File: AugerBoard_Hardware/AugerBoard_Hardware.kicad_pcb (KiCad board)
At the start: 2 copper layers, 88.9 x 82.5 mm, 51 parts, among them J1 RJ45_LED_Shielded, J2 Conn_01x04_MountingPin, Q1 BSS138, Q2 BSS138, Q3 BSS138, SW1 SW_SPDT, SW2 SW_Push, SW3 SW_Push, SW4 SW_Push, U1 Teensy4.1_DEV-16771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

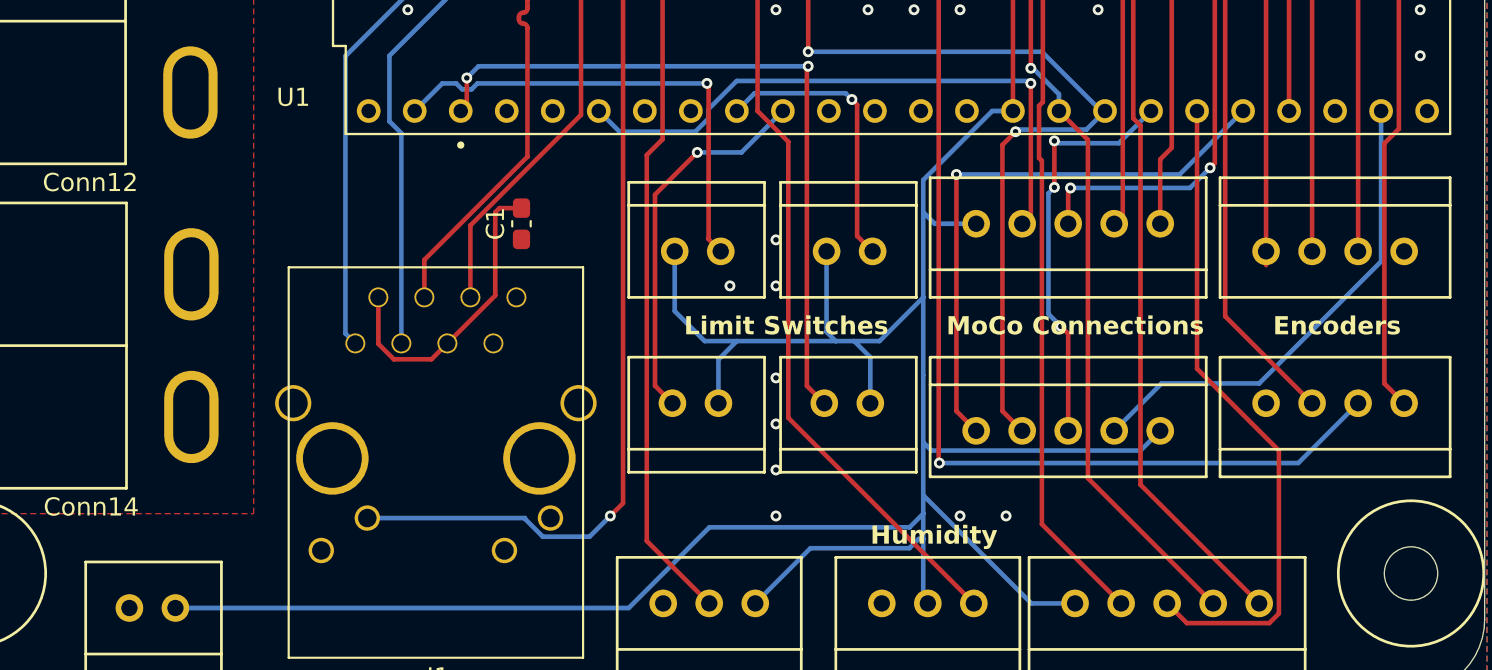
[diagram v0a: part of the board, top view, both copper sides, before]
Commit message: Flipped moco connector and traces, and added labels
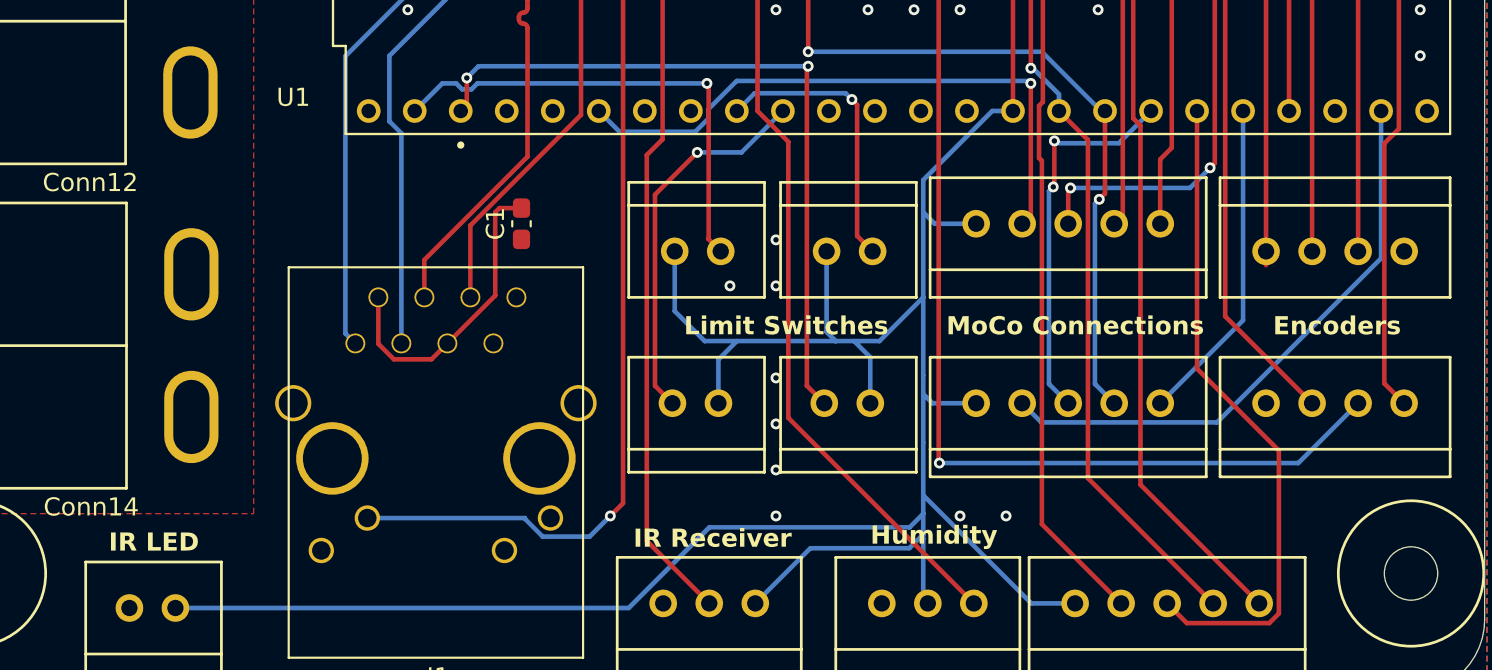
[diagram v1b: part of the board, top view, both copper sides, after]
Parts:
- moved Conn13 10.3 mm to (145.7, 138.6), turned to 180 degrees
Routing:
- net IN_B2: track 32.3 -> 18.5 mm, vias 1 -> 0
- net +3.3V: track 288.0 -> 277.5 mm
- net PWM2: track 81.4 -> 75.6 mm
- net IN_A2: track 26.9 -> 32.1 mm
- net CS2: track 22.7 -> 21.2 mm, vias 3 -> 2
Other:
- board text added: "IR LED"
- board text added: "IR Receiver"

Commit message: Flipped other moco gg
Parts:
- moved Conn9 10.3 mm to (135.5, 130.2), turned to 0 degrees
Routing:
- net +3.3V: track 277.5 -> 288.3 mm
- net IN_B1: track 39.1 -> 49.4 mm, vias 1 -> 3
- net IN_A1: track 33.8 -> 39.7 mm
- net PWM1: track 85.8 -> 82.5 mm
- net CS1: track 29.1 -> 31.4 mm
- net PWM3: track 76.3 -> 76.9 mm

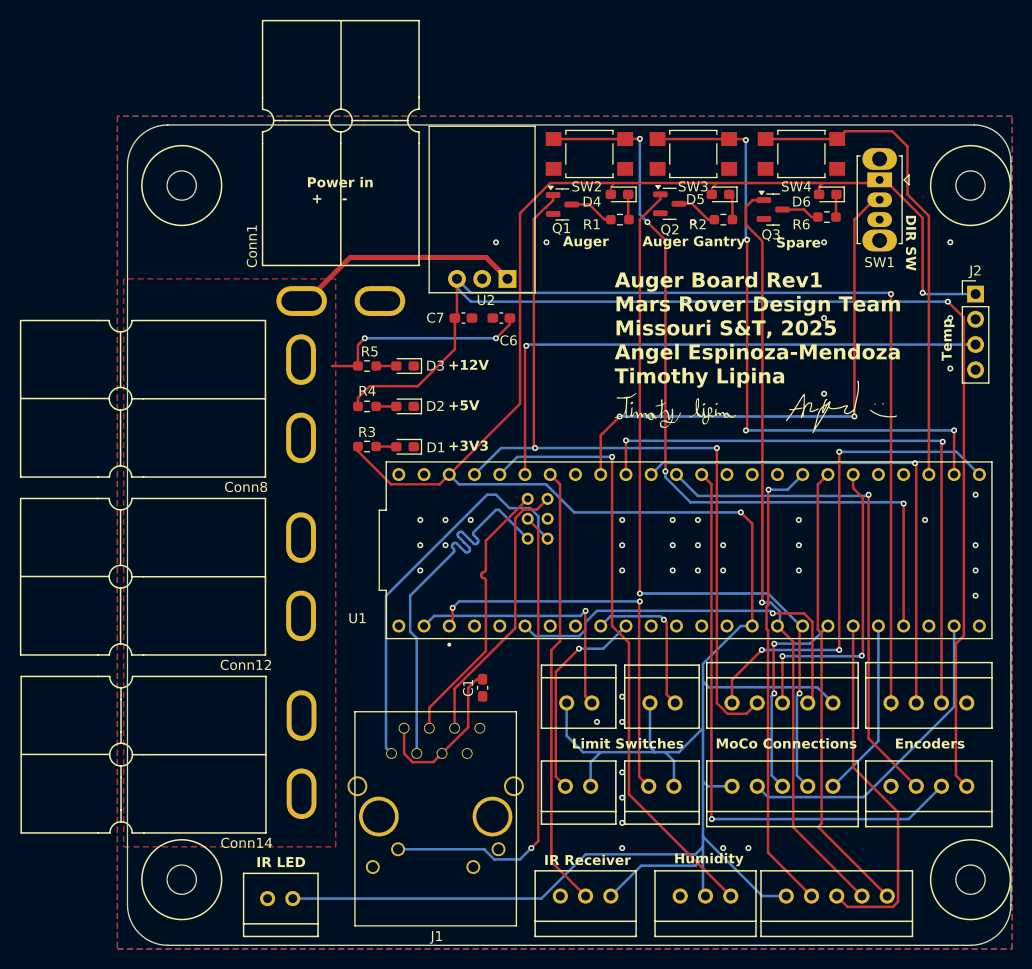
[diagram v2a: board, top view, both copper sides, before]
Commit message: Some layout review changes made
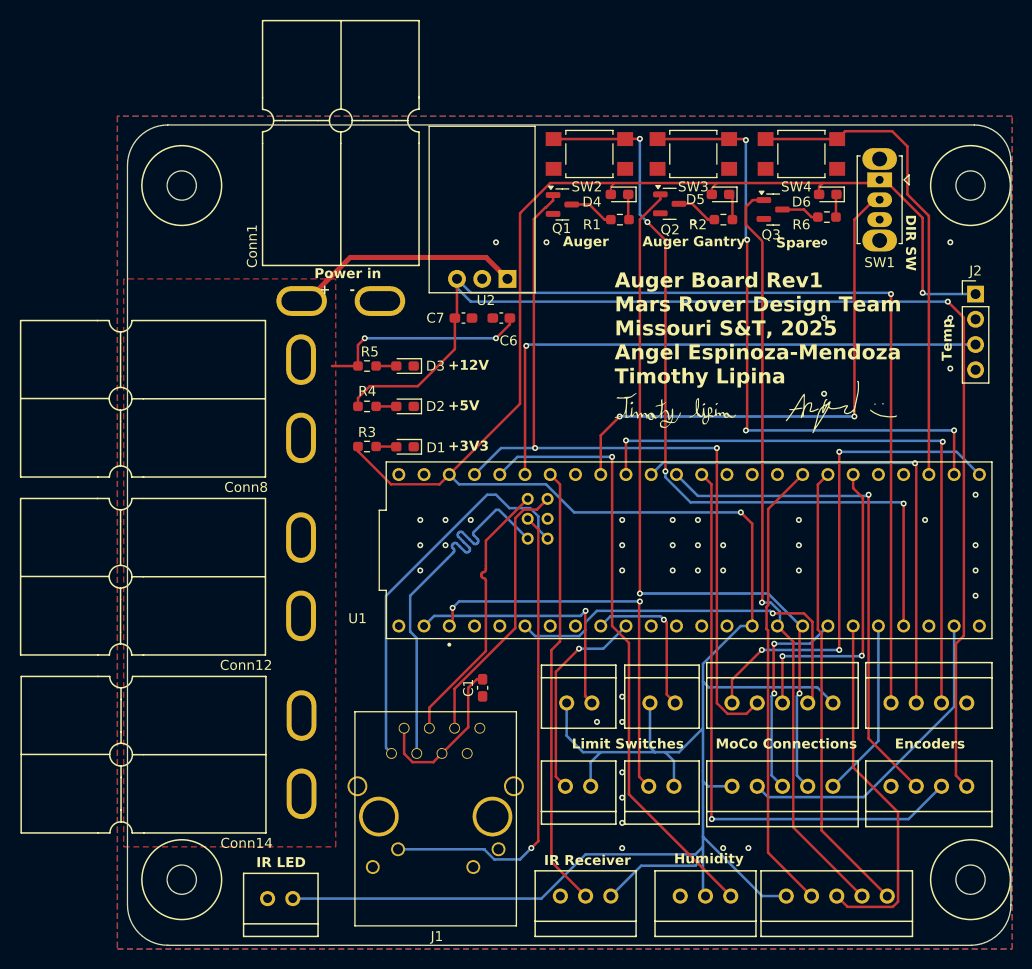
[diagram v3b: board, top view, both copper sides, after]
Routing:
- net IN_A3: track 46.9 -> 45.8 mm, vias 1 -> 0
- net +5V: track 207.1 -> 206.3 mm
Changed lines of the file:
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@@
 		(at 135.509 130.175)
 		(property "Reference" "Conn9"
-			(at -0.635 3.302 360)
+			(at -0.635 3.302 0)
 			(layer "F.SilkS")
 			(hide yes)
@@
 		)
 		(property "Value" "Molex_SL_05"
-			(at 5.08 3.302 360)
+			(at 5.08 3.302 0)
 			(layer "F.Fab")
 			(effects
@@
 		)
 		(property "Footprint" "MRDT_Connectors:MOLEX_SL_05_Vertical"
-			(at 0 0 360)
+			(at 0 0 0)
 			(layer "F.Fab")
 			(hide yes)
@@
 		)
 		(property "Datasheet" ""
-			(at 0 0 360)
+			(at 0 0 0)
 			(layer "F.Fab")
 			(hide yes)
@@
 		)
 		(property "Description" ""
-			(at 0 0 360)
+			(at 0 0 0)
 			(layer "F.Fab")
 			(hide yes)
@@
 	)
 	(gr_text "Power in\n +    -"
-		(at 92.71 80.01 0)
+		(at 93.472 89.154 0)
 		(layer "F.SilkS")
 		(effects
@@
 	)
 	(segment
-		(start 151.511 130.937)
-		(end 151.511 130.175)
-		(width 0.254)
-		(layer "F.Cu")
-		(net 4)
-	)
-	(segment
 		(start 107.622 94.562)
 		(end 103.886 98.298)
@@
 	)
 	(segment
-		(start 151.13 149.606)
-		(end 144.18 142.656)
+		(start 144.145 122.799344)
+		(end 144.145 108.204)
 		(width 0.254)
 		(layer "F.Cu")
@@
 	)
 	(segment
-		(start 144.18 142.656)
+		(start 144.526 143.002)
 		(end 144.526 142.31)
 		(width 0.254)
@@
 	)
 	(segment
-		(start 144.145 122.799344)
-		(end 144.145 108.204)
+		(start 144.526 142.31)
+		(end 144.526 123.180344)
 		(width 0.254)
 		(layer "F.Cu")
@@
 	)
 	(segment
-		(start 144.526 142.31)
-		(end 144.526 123.180344)
+		(start 151.13 149.606)
+		(end 144.526 143.002)
 		(width 0.254)
 		(layer "F.Cu")
@@
 	)
 	(segment
-		(start 143.51 149.606)
-		(end 139.138 145.234)
+		(start 139.138 145.234)
+		(end 139.138 122.882)
 		(width 0.254)
 		(layer "F.Cu")
@@
 	)
 	(segment
-		(start 139.138 122.882)
-		(end 138.981 122.725)
+		(start 139.154 110.655)
+		(end 142.621 107.188)
 		(width 0.254)
 		(layer "F.Cu")
@@
 	(segment
 		(start 139.154 120.327525)
-		(end 139.154 108.75)
-		(width 0.254)
-		(layer "F.Cu")
-		(net 22)
-	)
-	(segment
-		(start 139.154 108.75)
-		(end 139.192 108.712)
-		(width 0.254)
-		(layer "F.Cu")
-		(net 22)
-	)
-	(segment
-		(start 139.138 145.234)
-		(end 139.138 122.882)
+		(end 139.154 110.655)
 		(width 0.254)
 		(layer "F.Cu")
@@
 		(net 22)
 	)
-	(via
-		(at 139.192 108.712)
-		(size 0.6)
-		(drill 0.3)
-		(layers "F.Cu" "B.Cu")
-		(net 22)
-	)
 	(segment
-		(start 141.097 108.712)
-		(end 142.621 107.188)
+		(start 143.51 149.606)
+		(end 139.138 145.234)
 		(width 0.254)
-		(layer "B.Cu")
+		(layer "F.Cu")
 		(net 22)
 	)
 	(segment
-		(start 139.192 108.712)
-		(end 141.097 108.712)
+		(start 139.138 122.882)
+		(end 138.981 122.725)
 		(width 0.254)
-		(layer "B.Cu")
+		(layer "F.Cu")
 		(net 22)
 	)

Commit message: Layout Review Changes Made
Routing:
- net IN_A2: track 32.2 -> 35.9 mm
- net +3.3V: track 288.3 -> 291.5 mm
- net +5V: track 206.3 -> 207.7 mm
- net Encoder_1a: track 59.6 -> 60.4 mm
- net GND: vias 43 -> 149
- net CS2: vias 2 -> 3
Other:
- board text added: "CS2"
- board text added: "CS3"
- board text added: "Encdr1A"
- board text added: "Encdr1B"
- board text added: "Encdr2A"
- board text added: "Encdr2B"
- board text added: "IN_A2"
- board text added: "IN_A3"
- board text added: "IN_B2"
- board text added: "IN_B3"
- board text added: "MoCo Power + -"
- board text added: "PWM2"
- board text added: "PWM3"
- board text added: "VIR"
- board text removed: "Power in - +"

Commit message: FINAL Layout Changes probably
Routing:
- net GND: vias 149 -> 145
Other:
- board text added: "CS1"
- board text added: "E_1A"
- board text added: "E_1B"
- board text added: "E_2A"
- board text added: "E_2B"
- board text added: "Hum."
- board text added: "INA1"
- board text added: "INA2"
- board text added: "INA3"
- board text added: "INB1"
- board text added: "INB2"
- board text added: "INB3"
- board text added: "PWM1"
- board text removed: "Encdr1A"
- board text removed: "Encdr1B"
- board text removed: "Encdr2A"
- board text removed: "Encdr2B"
- board text removed: "IN_A2"
- board text removed: "IN_A3"
- board text removed: "IN_B2"
- board text removed: "IN_B3"
